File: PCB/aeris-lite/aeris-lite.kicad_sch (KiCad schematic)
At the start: 47 parts, among them J1 PMSA003A, J2 SHT45, J3 LPS22HB, J4 SCD40, J5 SGP41, J6 USB-C Input, J7 OUT, Q1 BSS138, Q2 BSS138, U1 ESP32-C6-SUPERMINI, U2 74AHCT244

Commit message: PCVB : Work in progress
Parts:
- removed H5: MountingHole, MountingHole:MountingHole_2.2mm_M2, symbol Mechanical:MountingHole
- removed J1: PMSA003A, esp32-h2-supermini:PLANTOWER_PMSA003-A, symbol Connector_Generic:Conn_02x05_Odd_Even
- removed J2: SHT45, esp32-h2-supermini:SHT45-Breakout, symbol Connector:Conn_01x04_Pin
- removed J3: LPS22HB, esp32-h2-supermini:LPS22HB-Breakout, symbol Connector:Conn_01x04_Pin
- removed J4: SCD40, esp32-h2-supermini:SCD40-Breakout, symbol Connector:Conn_01x04_Pin
- removed J5: SGP41, esp32-h2-supermini:SGP41-Breakout, symbol Connector:Conn_01x04_Pin
- removed J7: OUT, Connector_PinHeader_2.54mm:PinHeader_1x03_P2.54mm_Vertical, symbol Connector:Conn_01x03_Pin
- removed Q1, Q2: BSS138, Package_TO_SOT_SMD:SOT-23, symbol Transistor_FET:BSS138
- removed R10, R11, R12, R13: 47R, Resistor_SMD:R_0805_2012Metric, symbol Device:R
- removed R7, R8: 10K, Resistor_SMD:R_0805_2012Metric, symbol Device:R
- removed U2: 74AHCT244, Package_SO:SOIC-20W_7.5x12.8mm_P1.27mm, symbol 74xx:74AHCT244
- added C11: 100µF, Capacitor_SMD:CP_Elec_6.3x5.9, symbol Device:C_Polarized_Small
- added C12, C13, C14: 0.1µF, Capacitor_SMD:C_0805_2012Metric, symbol Device:C
- added C15, C16: 1µF, Capacitor_SMD:C_0805_2012Metric, symbol Device:C
- added Sen1: SCD4x, Sensor:Sensirion_SCD4x-1EP_10.1x10.1mm_P1.25mm_EP4.8x4.8mm, symbol SCD41-D-R1:SCD4x
- added U2: 74AHC1G125, Package_TO_SOT_SMD:SOT-23-5, symbol 74xGxx:74AHC1G125
- added U4: SHT4x, Sensor_Humidity:Sensirion_DFN-4_1.5x1.5mm_P0.8mm_SHT4x_NoCentralPad, symbol Sensor_Humidity:SHT4x
- added U6: DPS368XTSA1, DPS368XTSA1:XDCR_DPS368XTSA1, symbol DPS368XTSA1:DPS368XTSA1
- added U7: SGP41-D-R4, SGP41-D-R4:XDCR_SGP41-D-R4, symbol SGP41-D-R4:SGP41-D-R4
- C1, C4: footprint Capacitor_SMD:C_1206_3216Metric -> Capacitor_SMD:C_0805_2012Metric
- R1, R2: value 4.7K -> 10K
- R3: value 10K -> 330R
- R6: value 10K -> 4.7R
- R9: value 47R -> 470R
- renumbered D5 to D3, D3 to D4, D4 to D5
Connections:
- net +3V3: now also R4.1, R5.2, C12.1, C13.1, C14.1, C15.1, Sen1.7 (VDD), U4.3 (VDD), U6.8 (VDD), U7.1 (VDD); no longer R3.2, R4.2, R5.1, R6.1
- net +5V: now also C11.1, U2.5 (VCC)
- net GND: now also C11.2, C12.2, C13.2, C14.2, C15.2, Sen1.20 (VSS), Sen1.21 (VSS), Sen1.6 (VSS), U2.1, U2.3 (GND), U4.4 (VSS), U6.1 (GND), U6.7 (GND), U7.2 (VSS)
- net at D5.3 (DIN): now also D4.1 (DOUT)
- net at D2.1 (DOUT): now also D3.3 (DIN)
- net at D2.3 (DIN): now also D1.1 (DOUT)
- net at D3.1 (DOUT): now also D4.3 (DIN)
- net CO2: no longer names the net of R9.1
- net CO2: now also U2.4
- net GPIO0: no longer names the net of U1.18 (IO0)
- net GPIO0: no longer R5.2
- net GPIO1: no longer names the net of U1.17 (IO1)
- net GPIO14 renamed SDA_0
- net SDA_0: now also R1.2, Sen1.10 (SDA), U7.3 (SDA)
- net GPIO15 renamed SCL_0
- net SCL_0: now also R2.1, Sen1.9 (SCL), U7.6 (SCL)
- net GPIO18: no longer names the net of U1.5 (IO18)
- net GPIO19: no longer names the net of U1.6 (IO19)
- net GPIO19: no longer R4.1
- net GPIO20: no longer names the net of U1.7 (IO20)
- net GPIO3: no longer names the net of R6.2
- net GPIO3: no longer U1.15 (IO3)
- net RX: no longer names the net of U1.13 (IO5)
- net SCL: no longer names the net of U1.11 (IO7)
- net SCL: no longer R2.1
- net SDA: no longer names the net of U1.12 (IO6)
- net SDA: no longer R1.2
- net TX renamed SCL_1
- net SCL_1: now also R5.1, U4.2 (SCL), U6.4 (SCK)
- new net: R3.2, U2.2
- new net SDA_1: R4.2, U1.15 (IO3), U4.1 (SDA), U6.3 (SDI)
- no-connect marks 24 -> 20
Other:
- note added: "Status"
- note removed: "Bi-directional Level Shifter"
- note removed: "PLANTOWER PMSA003-A"
- note removed: "PM2.5"
- moved on the sheet: C1, C10, C2, C3, C4, C5, C6, C7, C8, C9, D0, D1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

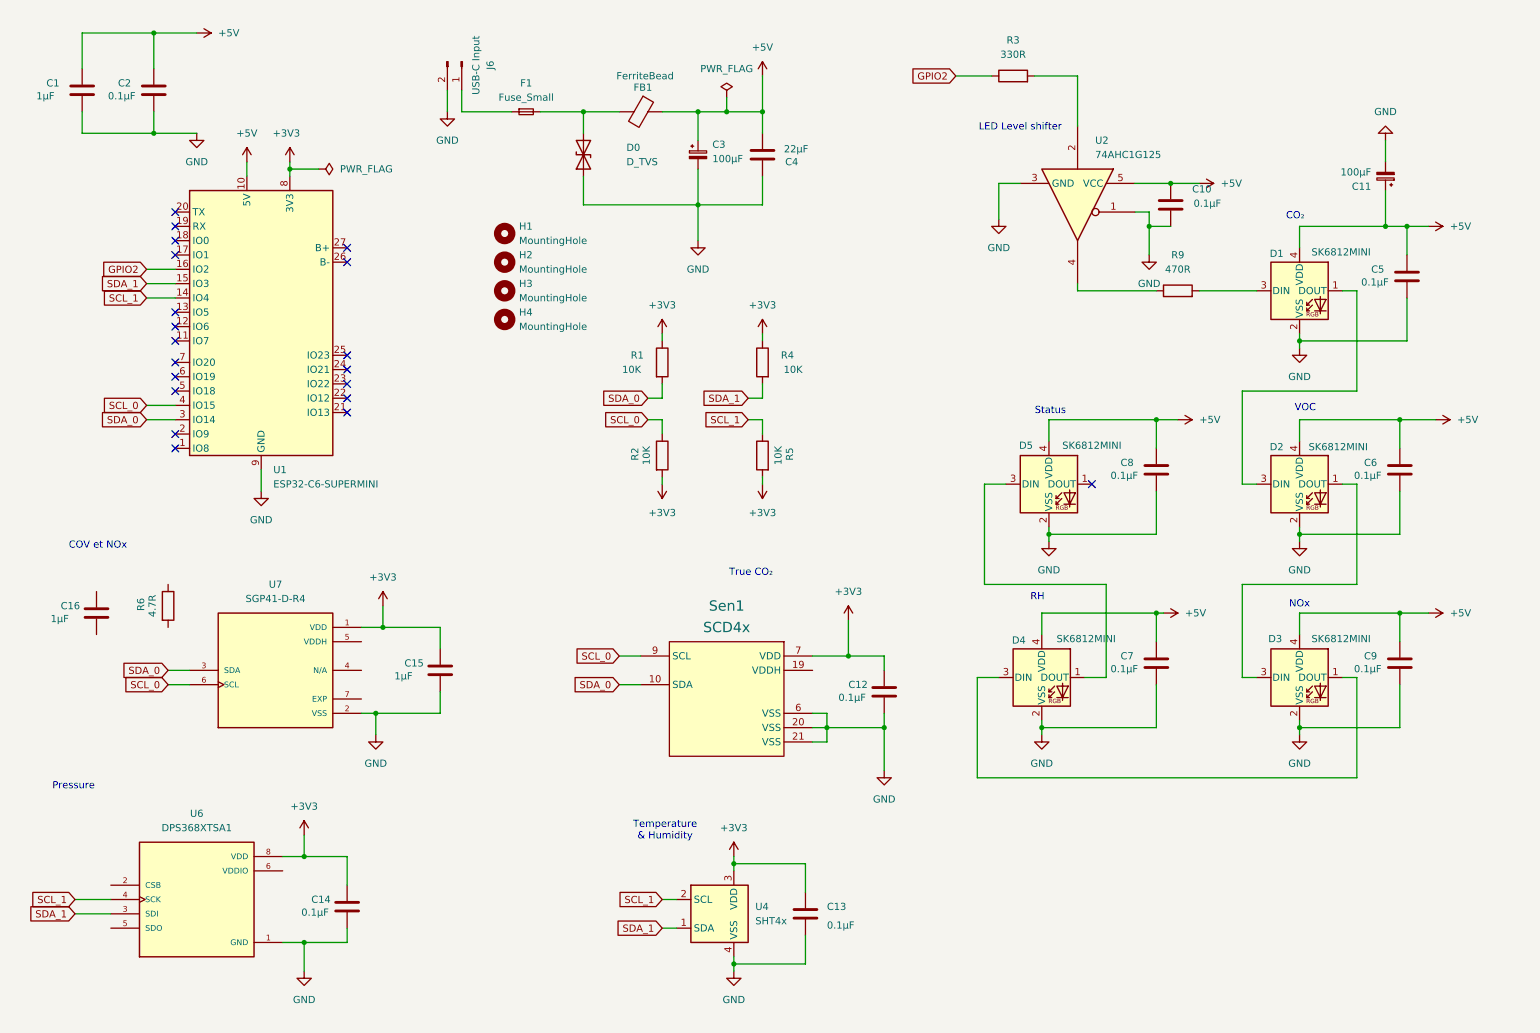
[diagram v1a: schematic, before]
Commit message: feat: Implement fan control driver for Aeris_Lite
- Added fan_control.c and fan_control.h to manage PWM speed control and RPM monitoring for a 5V 4-wire PWM fan.
- Integrated GPIO configuration for fan power control and tachometer pulse counting.
- Implemented functions for initializing the fan system, setting power and speed, retrieving RPM, and checking fan status.
- Added adaptive control based on temperature and air quality sensor readings.
- Defined fan operating modes and status structure for better management and monitoring.
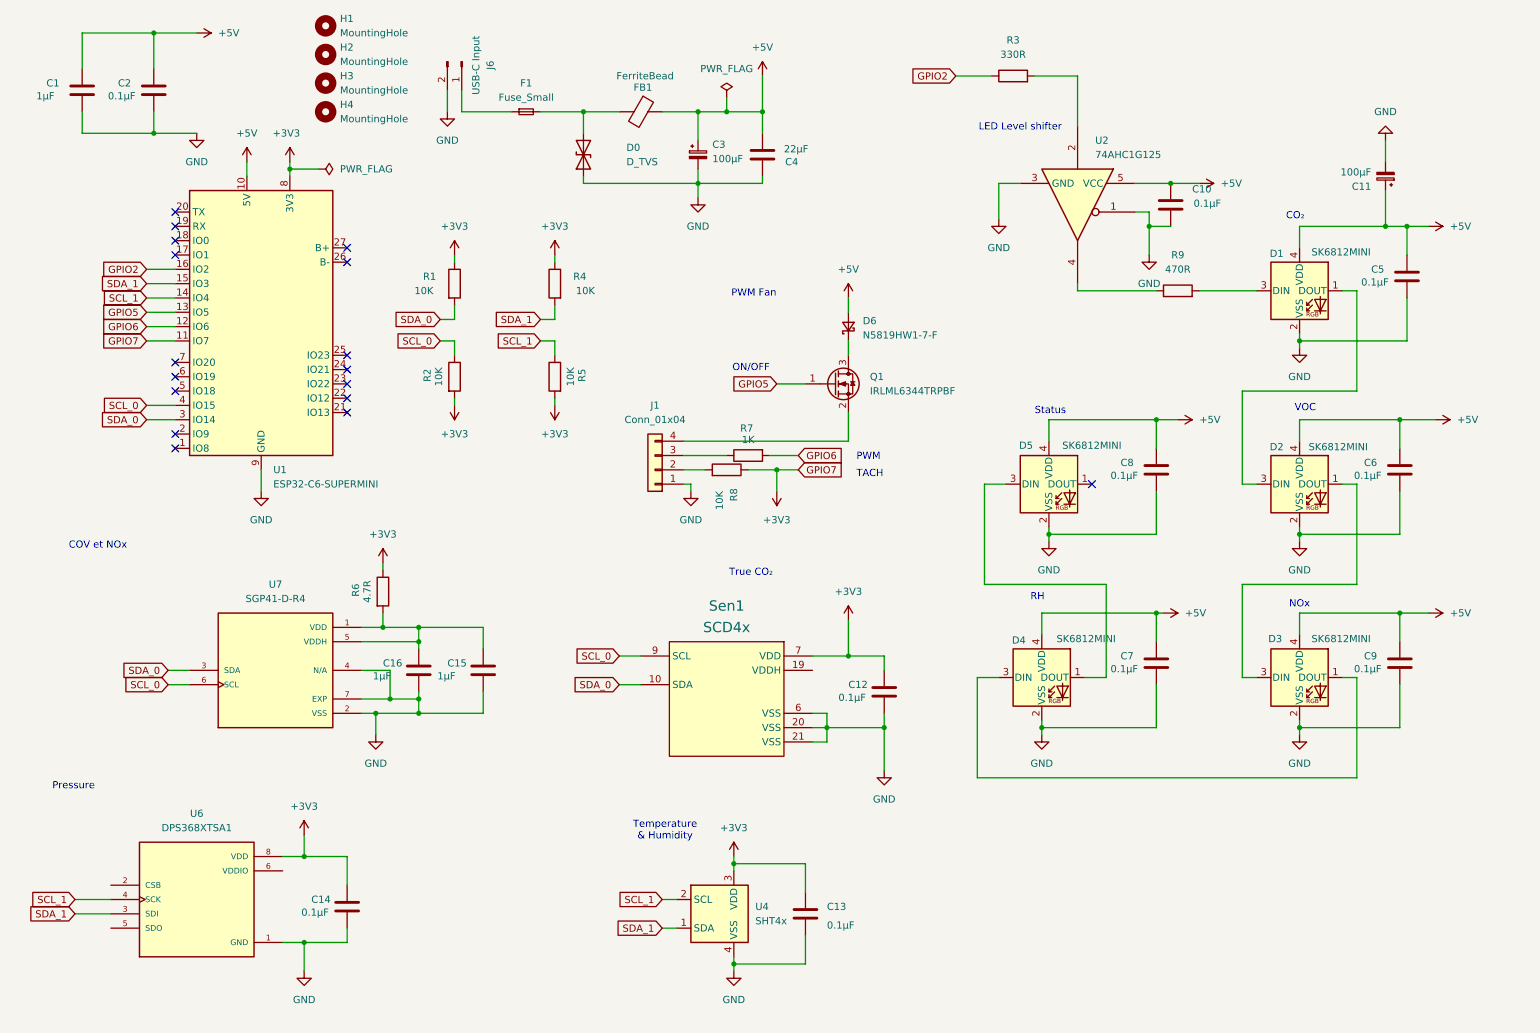
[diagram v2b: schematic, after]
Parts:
- added D6: N5819HW1-7-F, Diode_SMD:D_SOD-123F, symbol Device:D_Schottky_Small
- added J1: Conn_01x04, Connector_JST:JST_GH_SM04B-GHS-TB_1x04-1MP_P1.25mm_Horizontal, symbol Connector_Generic:Conn_01x04
- added Q1: IRLML6344TRPBF, Package_TO_SOT_SMD:SOT-23, symbol Transistor_FET:Q_NMOS_GSD
- added R7: 1K, Resistor_SMD:R_0805_2012Metric, symbol Device:R
- added R8: 10K, Resistor_SMD:R_0805_2012Metric, symbol Device:R
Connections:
- net +3V3: now also R6.1, U1.11 (IO7), R8.1; no longer C15.1, U7.1 (VDD)
- net +5V: now also D6.2 (A)
- net GND: now also C16.2, U7.4 (N/A), U7.7 (EXP), J1.1 (Pin_1)
- net at R6.2: now also C15.1, C16.1, U7.1 (VDD), U7.5 (VDDH)
- net GPIO6: now reaches U1.12 (IO6)
- net GPIO6: now also R7.2
- net GPIO5: now reaches U1.13 (IO5)
- net GPIO5: now also Q1.1 (G)
- new net: J1.4 (Pin_4), Q1.2 (S)
- new net: D6.1 (K), Q1.3 (D)
- new net: J1.2 (Pin_2), R8.2
- new net: J1.3 (Pin_3), R7.1
- no-connect marks 20 -> 17
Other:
- note added: "ON/OFF"
- note added: "PWM"
- note added: "PWM Fan"
- note added: "TACH"
- moved on the sheet: C15, C16, H1, H2, H3, H4, R1, R2, R4, R5, R6
